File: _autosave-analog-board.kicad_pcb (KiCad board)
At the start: 2 copper layers, 200 x 150 mm, 459 parts, among them J1 AC IN, J2 OUT, J3 CONN_20X2, P2 CONN_01X02, Q1 2N3906, Q10 2N3906, Q11 2N3906, Q12 2N3906, Q13 2N3906, Q14 2N3906, Q15 2N3906, Q16 2N3906, Q17 NPN, Q18 NPN, Q19 J111, Q2 2N3906, Q20 2N3906, Q3 2N3906, Q4 2N3906, Q5 2N3906, Q6 BCM857BS, Q7 2N3906, Q8 2N3906, Q9 2N3906, U1 LM13700, U10 ADR01, U11 DG212B, U12 DG212B, U13 DG408, U14 DG408, U15 TL072-, U16 DG408, U17 DG408, U18 LM13700, U19 LM13700, U2 LM13700, U21 TL072-, U22 TL074-, U23 TL074-, U24 TL074-, U25 TL074-, U26 TL072-, U27 TL074-, U28 TL074-, U29 LM13700, U3 LM13700, U30 LM13700, U31 TL074-, U32 LM13700, U33 TL074-, U34 TL074-, U35 TL074-, U36 74LV573, U38 0 - 10V, U39 TL074-, U4 DG212B, U40 DG419, U41 0 - 10V, U42 10 - 0V, U43 LM7812, U44 LM7912, U45 DG408, U46 7805, U5 TL074-, U6 AD5556, U7 TL072-, U8 TL074-, U9 AD8672

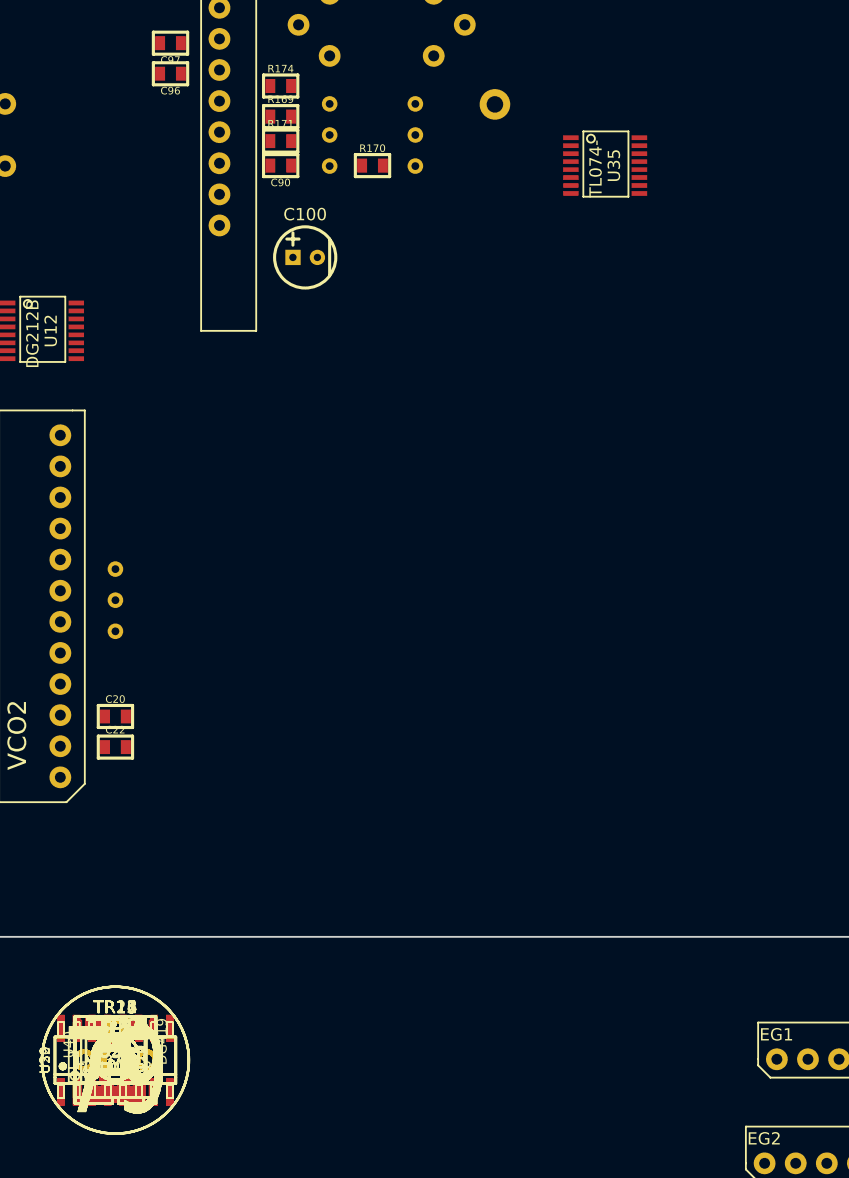
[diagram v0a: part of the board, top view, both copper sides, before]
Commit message: analog board component placement. problem with tssop-14 footprint. public kicad github repository seems to have dropped this footprint
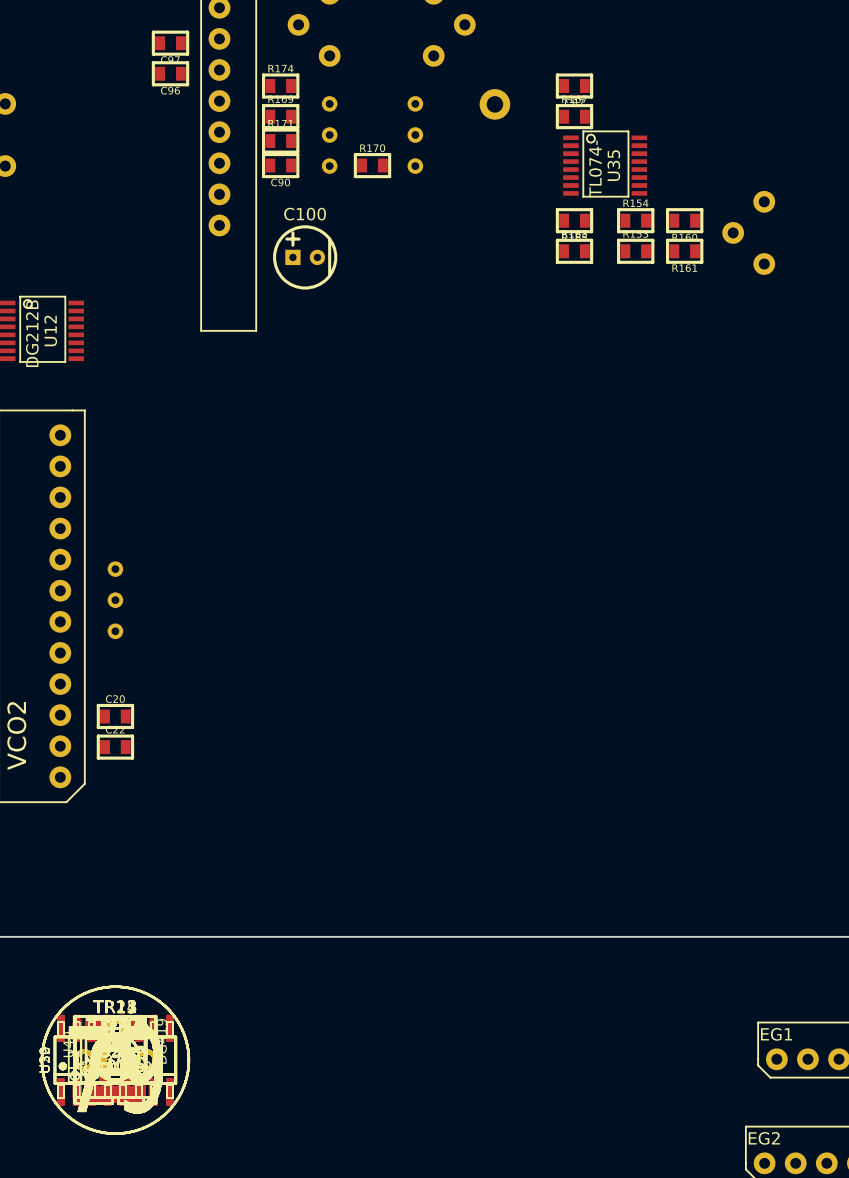
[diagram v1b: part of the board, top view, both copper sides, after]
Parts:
- TR16: moved to B.Cu
- moved C87 88.0 mm to (137.5, 80.5), turned to 180 degrees
- moved TR16 85.9 mm to (153.0, 92.5), turned to 270 degrees
- moved R167 85.7 mm to (137.5, 83.0)
- moved R160 82.9 mm to (146.5, 91.5), turned to 180 degrees
- moved R161 80.8 mm to (146.5, 94.0), turned to 180 degrees
- moved R154 80.7 mm to (142.5, 91.5)
- moved R153 78.6 mm to (142.5, 94.0)
- moved R165 78.2 mm to (137.5, 91.5), turned to 180 degrees
- moved R163 76.0 mm to (137.5, 94.0)
